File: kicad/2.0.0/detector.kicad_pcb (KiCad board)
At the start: 4 copper layers, 33 x 29.3 mm, 45 parts, among them J1 Conn_01x05_Male, J2 Conn_01x05_Male, U1 LT1761-5, U2 LT1964-5, U3 REF5010ID, U4 OPA2197xD, U5 OPA2197xD

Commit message: reworked detector 2.0.0 pcb
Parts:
- removed REF** (x2): MountingHole_2.7mm_M2.5_ISO7380_Pad, MountingHole:MountingHole_2.7mm_M2.5_ISO7380_Pad
- added M2.5: MountingHole_2.7mm_M2.5_ISO7380_Pad, MountingHole:MountingHole_2.7mm_M2.5_ISO7380_Pad, F.Cu at (180.7, 116.4)
- added M2.5: MountingHole_2.7mm_M2.5_ISO7380_Pad, MountingHole:MountingHole_2.7mm_M2.5_ISO7380_Pad, F.Cu at (148.2, 116.4)
- moved C1 65.5 mm to (176.3, 126.7), turned to 0 degrees
- moved C3 64.0 mm to (176.3, 125.1), turned to 0 degrees
- moved TP19 63.1 mm to (174.1, 131.2)
- moved U1 61.3 mm to (176.5, 122.1), turned to 90 degrees
- moved C6 58.5 mm to (176.3, 119.1), turned to 180 degrees
- moved C13 58.0 mm to (176.8, 141.4), turned to 270 degrees
- moved C8 57.8 mm to (173.2, 120.7), turned to 270 degrees
- moved TP15 57.7 mm to (154.6, 147.2)
- moved M2.5 57.7 mm to (180.7, 147.3)
- moved J2 57.5 mm to (180.7, 139.5)
- moved C2 57.1 mm to (167.7, 125.7), turned to 0 degrees
- moved C16 56.3 mm to (172.0, 143.7)
- moved U4 56.1 mm to (173.3, 139.2)
- moved R4 56.1 mm to (172.0, 145.3)
- moved C15 55.9 mm to (158.6, 141.4), turned to 270 degrees
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- renumbered REF** to M2.5
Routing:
- net -5V: track 50.0 -> 10.5 mm, vias 3 -> 0
- net +5V: track 50.0 -> 10.6 mm, vias 3 -> 0
- net GND: track 57.6 -> 20.9 mm, vias 7 -> 0
- net /-Y1: track 35.4 -> 3.67 mm, vias 1 -> 0
- net /-X2: track 30.7 -> 3.69 mm, vias 1 -> 0
- net -12V: track 28.7 -> 6.53 mm, vias 2 -> 0
- net Net-(C16-Pad2): track 23.5 -> 5.64 mm
- net /-X1: track 21.3 -> 3.69 mm, vias 1 -> 0
- net +12V: track 33.3 -> 16.8 mm, vias 3 -> 0
- net Net-(C18-Pad2): track 19.8 -> 5.56 mm
- net Net-(C19-Pad2): track 18.6 -> 5.62 mm
- net Net-(C17-Pad2): track 18.0 -> 7.20 mm
- net /-Y2: track 14.4 -> 3.64 mm, vias 1 -> 0
- net Net-(C11-Pad1): track 15.5 -> 5.43 mm
- net Net-(C7-Pad2): track 4.78 -> 5.85 mm
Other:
- board size 33 x 29.3 mm -> 38.6 x 37.2 mm

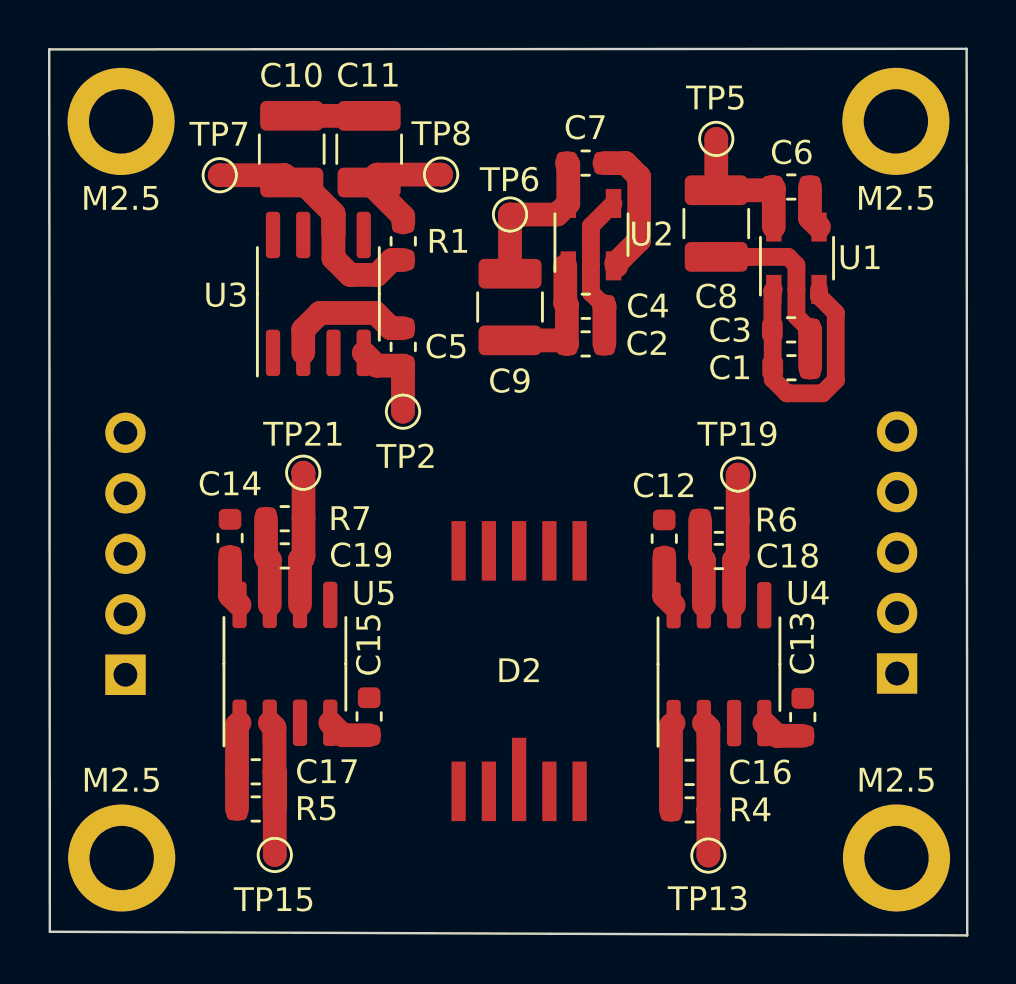
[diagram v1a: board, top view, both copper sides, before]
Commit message: completed redesign of arithmetic and detector 2.0.0 boards
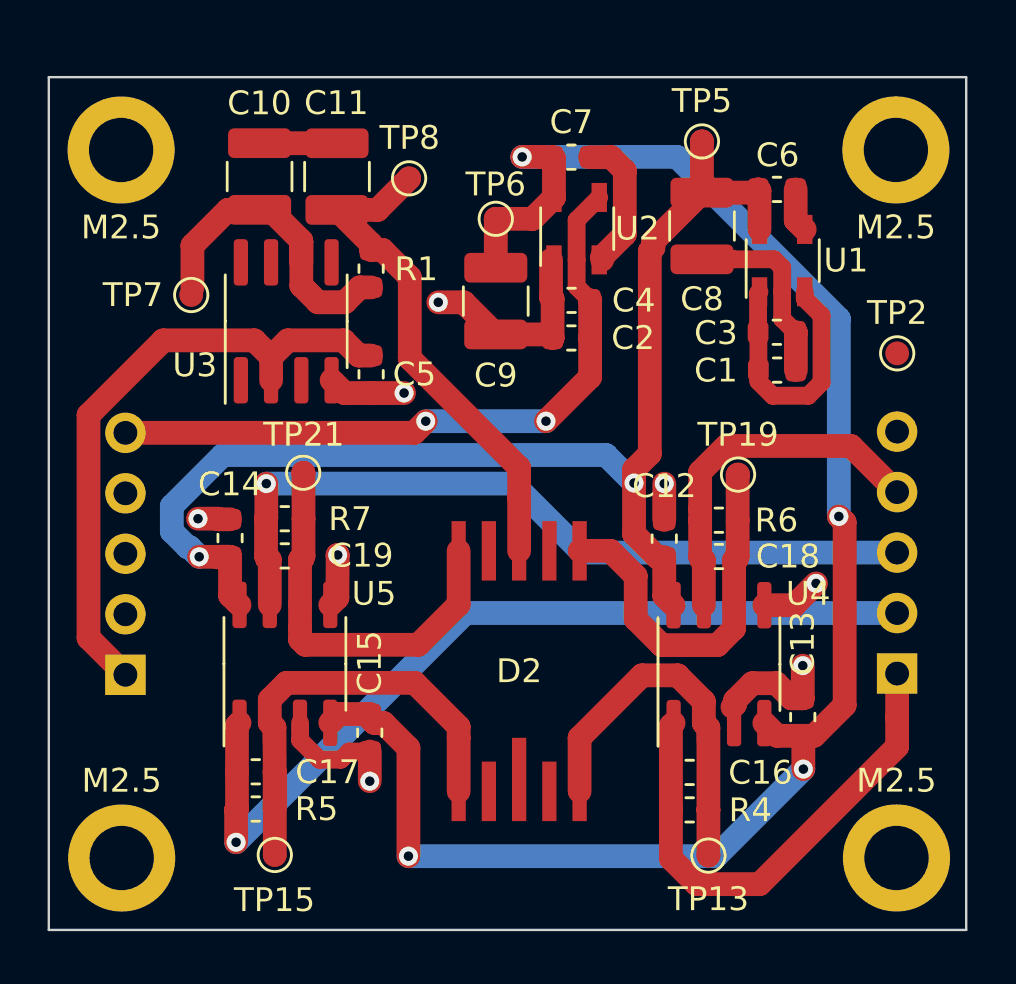
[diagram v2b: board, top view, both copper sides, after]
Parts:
- removed the M2.5 at (180.7, 116.4)
- removed the M2.5 at (148.2, 116.4)
- added M2.5: MountingHole_2.7mm_M2.5_ISO7380_Pad, MountingHole:MountingHole_2.7mm_M2.5_ISO7380_Pad, F.Cu at (180.7, 117.6)
- added M2.5: MountingHole_2.7mm_M2.5_ISO7380_Pad, MountingHole:MountingHole_2.7mm_M2.5_ISO7380_Pad, F.Cu at (148.2, 117.6)
- moved TP2 20.9 mm to (180.8, 126.1), turned to 270 degrees
- moved TP7 5.17 mm to (151.1, 123.7), turned to 270 degrees
- moved C11 1.77 mm to (157.2, 118.7)
- moved C5 1.77 mm to (158.7, 127.0)
- moved R1 1.77 mm to (158.7, 122.5)
- moved C10 1.77 mm to (154.0, 118.7)
- moved U3 1.77 mm to (155.1, 124.8)
- moved TP8 1.35 mm to (160.2, 118.8)
- moved C15 0.69 mm to (158.6, 142.0), turned to 90 degrees
- moved C4 0.65 mm to (167.1, 123.9)
- moved C2 0.65 mm to (167.1, 125.5)
- moved C7 0.65 mm to (167.1, 117.9)
- moved C9 0.65 mm to (163.9, 123.9)
- moved U2 0.65 mm to (167.3, 120.9)
- moved TP6 0.63 mm to (163.9, 120.5)
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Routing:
- net -5V: track 10.5 -> 72.6 mm, vias 0 -> 4
- net +5V: track 10.6 -> 53.1 mm, vias 0 -> 2
- net /-Y1: track 3.67 -> 36.8 mm, vias 0 -> 1
- net /-X2: track 3.69 -> 32.9 mm, vias 0 -> 1
- net -12V: track 6.53 -> 28.7 mm, vias 0 -> 2
- net +12V: track 16.8 -> 37.6 mm
- net GND: track 20.9 -> 41.5 mm, vias 0 -> 8
- net /-X1: track 3.69 -> 21.1 mm
- net Net-(C11-Pad1): track 5.43 -> 21.3 mm
- net Net-(C17-Pad2): track 7.20 -> 19.9 mm
- net /-Y2: track 3.64 -> 15.2 mm
- net Net-(C19-Pad2): track 5.62 -> 16.8 mm
- net Net-(C18-Pad2): track 5.56 -> 16.0 mm
- net Net-(C16-Pad2): track 5.64 -> 15.6 mm
- net Net-(C10-Pad1): track 11.7 -> 13.7 mm
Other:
- board size 38.6 x 37.2 mm -> 38.5 x 35.8 mm
